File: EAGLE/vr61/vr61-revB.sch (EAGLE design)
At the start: 235 parts, among them J2 SM04B-SRSS-TB(LF)(SN), J6 MICROMOD-2222-C, Y1 74AHCT1G125

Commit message: wip 2022-07-21
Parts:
- removed J6: MICROMOD-2222-C, SparkFun-MicroMod:MICROMOD-2222-C
- added C12: 1mF, rcl:C-EUC0603
- added C13: 100nF, rcl:C-EUC0603
- added R7: 470, rcl:R-EU_R0603
- added R8: 5.1K, rcl:R-EU_R0603
- added W1: M25C, __untitled:M25C
- added X1: MICROMOD-2222-C, SparkFun-MicroMod:MICROMOD-2222-C
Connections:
- removed net N$70: LED-CL.4_DIN, Y1.Y_DOUT
- new net EE_CS: W1.!CS, X1.SPI_!CS!
- new net MISO: W1.DO, X1.SPI_SDI
- new net MOSI: W1.DIO, X1.SPI_SDO
- new net N$66: R7.2, Y1.Y_DOUT
- new net N$67: LED-CL.4_DIN, R7.1
- new net SCK: R8.2, W1.CLK, X1.SPI_SCK
- net !BOOT: now also X1.!BOOT!; no longer J6.!BOOT!
- net !RESET: now also X1.!RESET!; no longer J6.!RESET!
- net A0: now also X1.A0; no longer J6.A0
- net D+: now also X1.USB_D+; no longer J6.USB_D+
- net D-: now also X1.USB_D-; no longer J6.USB_D-
- net GND: now also C12.2, C13.2, R8.1, W1.GND, X1.GND; no longer J6.GND
- net LED: now also X1.PWM1; no longer J6.PWM1
- net MX0: now also X1.D1/CAM_TRIG; no longer J6.D1/CAM_TRIG
- net MX1: now also X1.I2C_!INT!; no longer J6.I2C_!INT!
- net MX2: now also X1.I2C_SCL; no longer J6.I2C_SCL
- net MX3: now also X1.A1; no longer J6.A1
- net MX4: now also X1.I2C_SDA; no longer J6.I2C_SDA
- net MX5: now also X1.D0; no longer J6.D0
- net MX6: now also X1.TX1; no longer J6.TX1
- net MX7: now also X1.RX1; no longer J6.RX1
- net MY0: now also X1.AUD_OUT/CAM_MCLK; no longer J6.AUD_OUT/CAM_MCLK
- net MY1: now also X1.AUD_IN/CAM_PCLK; no longer J6.AUD_IN/CAM_PCLK
- net MY2: now also X1.AUD_LRCLK; no longer J6.AUD_LRCLK
- net MY3: now also X1.AUD_BCLK; no longer J6.AUD_BCLK
- net MY4: now also X1.G4/BUS4; no longer J6.G4/BUS4
- net MY5: now also X1.G3/BUS3; no longer J6.G3/BUS3
- net MY6: now also X1.G2/BUS2; no longer J6.G2/BUS2
- net MY7: now also X1.G1/BUS1; no longer J6.G1/BUS1
- net MY8: now also X1.G0/BUS0; no longer J6.G0/BUS0
- net PWM: now also X1.PWM0; no longer J6.PWM0
- net SWDCK: now also X1.SWDCK; no longer J6.SWDCK
- net SWDIO: now also X1.SWDIO; no longer J6.SWDIO
- net VCC: now also C13.1, W1.!HLD, W1.!WP, W1.VCC, X1.3.3V, X1.3.3V_EN; no longer J6.3.3V, J6.3.3V_EN
- net VIN/3: now also X1.BATT_VIN/3; no longer J6.BATT_VIN/3
- net VSUP: now also C12.1, X1.USB_VIN; no longer J6.USB_VIN
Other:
- note added: "SPI EEPROM"
- moved on the sheet: C1, C10, C11, C2, C3, C4, C5, C7, C8, C9, D0, H5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

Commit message: wip 2022-07-21
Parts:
- removed Y1: 74AHCT1G125, ts_keyboards:74AHCT1G125
- removed Z1, Z10, Z11, Z12, Z13, Z16, Z17, Z18, Z19, Z2, Z20, Z21, Z22, Z23, Z24, Z25, Z26, Z27, Z3, Z30, Z31, Z32, Z33, Z34, Z35, Z36, Z37, Z38, Z39, Z4, Z40, Z43, Z44, Z45, Z46, Z47, Z48, Z49, Z5, Z50, Z51, Z52: MX-FPRINT-100U19, ts_keyboards:MX-FPRINT-100U19
- removed Z14: MX-FPRINT-200U19, ts_keyboards:MX-FPRINT-200U19
- removed Z15, Z28: MX-FPRINT-150U19, ts_keyboards:MX-FPRINT-150U19
- removed Z29: MX-FPRINT-175U19, ts_keyboards:MX-FPRINT-175U19
- removed Z41, Z42: MX-FPRINT-225U19, ts_keyboards:MX-FPRINT-225U19
- removed Z53: MX-FPRINT-275U19, ts_keyboards:MX-FPRINT-275U19
- removed Z54, Z55, Z56, Z58, Z59, Z60, Z61: MX-FPRINT-125U19, ts_keyboards:MX-FPRINT-125U19
- removed Z57: MX-FPRINT-625U19, ts_keyboards:MX-FPRINT-625U19
- added IC1: MC74VHC1G50SC-74A, ts_keyboards:MC74VHC1G50SC-74A
- renumbered B14 to T_BSPC, B41 to T_ENT, B42 to T_LSFT, B53 to T_RSFT, B57 to T_SPC, S_BSL to S_BSLS, S_BSP to S_BSPC, S_CB to S_RBRC, S_CPS to S_CAPS, S_FSL to S_SLSH, S_LAL to S_LALT, S_LCT to S_LCTL, S_LGU to S_LGUI, S_LSH to S_LSFT, S_MIN to S_MINS, S_OB to S_LBRC, S_QUO to S_QUOT, S_RAL to S_APP, S_RCT to S_RCTL, S_RGU to S_RALT, S_RSH to S_RSFT, S_SCL to S_SCLN
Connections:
- net GND: now also IC1.3_GND; no longer Y1.!OE, Y1.3_GND
- net LED1ST: now also IC1.A_DIN; no longer Y1.A_DIN
- net N$66: now also IC1.Y_DOUT; no longer Y1.Y_DOUT
- net VSUP: now also IC1.5_VCC; no longer Y1.5_VCC

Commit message: wip 2022-07-22
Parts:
- removed SA1, SA2, SA3, SC2: MOUNTING-HOLE-WIDE, ts_keyboards:MOUNTING-HOLE-WIDE
- removed SC1: MOUNTING-HOLE, ts_keyboards:MOUNTING-HOLE
- removed SG1, SG4: MOUNTING-HOLE-VWIDEEDGE-CUT, ts_keyboards:MOUNTING-HOLE-VWIDEEDGE-CUT
- added FP_AP2: FOOTPRINT-AP2, ts_keyboards:FOOTPRINT-AP2
- added FP_GH60: FOOTPRINT-GH60, ts_keyboards:FOOTPRINT-GH60
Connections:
- removed net SA1: SA1.P$1
- removed net SA2: SA2.P$1
- removed net SA3: SA3.P$1
- removed net SC2: SC2.P$1
- removed net SG1: SG1.P$1
- removed net SG4: SG4.P$1
- net SC1: no longer SC1.P$1
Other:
- note added: "TE P# 2199119-4"
- moved on the sheet: J3, JP2

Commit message: final touches and validation for rev B
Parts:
- removed IC1: MC74VHC1G50SC-74A, ts_keyboards:MC74VHC1G50SC-74A
- added D62: (no value), jlcpcb_basic_parts:1N5819WS
- added J6: (no value), SparkFun-Connectors:CONN_01
- added J7: (no value), SparkFun-Connectors:CONN_02
- added S_BSLS2, S_ENT2, S_LSFT2, S_NUBS: MX-5-PIN-HOTSWAP-PADNO-SILK, ts_keyboards:MX-5-PIN-HOTSWAP-PADNO-SILK
- added T_ENT1: MX-STABS-200U, ts_keyboards:MX-STABS-200U
- added U$14: 74AHCT1G125GV, ts_keyboards:74AHCT1G125GV
- J3: device SparkFun-Connectors:CONN_04 -> SparkFun-Connectors:CONN_03
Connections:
- removed net A0: J3.3, X1.A0
- removed net PWM: J3.2, X1.PWM0
- removed net SINK: LM1117.OUT@1
- removed net SWDCK: X1.SWDCK
- removed net SWDIO: X1.SWDIO
- new net 52: J3.2, X1.AUD_LRCLK
- new net 63: J6.1, X1.G10/ADC_D+/CAM_VSYNC
- new net N$69: D43.A, S_NUBS.P
- new net USBHOST_D+: J7.1, X1.USBHOST_D+
- new net USBHOST_D-: J7.2, X1.USBHOST_D-
- net GND: now also U$14.!OE, U$14.3_GND; no longer IC1.3_GND
- net LED: now also X1.PWM0; no longer X1.PWM1
- net LED1ST: now also U$14.A_DIN; no longer IC1.A_DIN
- net MX0: now also D50.C, D55.C, X1.PWM1; no longer D49.C, D54.C, X1.D1/CAM_TRIG
- net MX1: now also D43.C, D51.C, D56.C, X1.RX1; no longer D50.C, D55.C, X1.I2C_!INT!
- net MX2: now also D44.C, D52.C, D57.C, X1.TX1; no longer D43.C, D51.C, D56.C, X1.I2C_SCL
- net MX3: now also D45.C, D53.C, D58.C, X1.D1/CAM_TRIG; no longer D44.C, D52.C, D57.C, X1.A1
- net MX4: now also D46.C, D59.C, X1.I2C_!INT!; no longer D45.C, D58.C, X1.I2C_SDA
- net MX5: now also D47.C, D54.C, D60.C, X1.I2C_SCL; no longer D46.C, D53.C, D59.C, X1.D0
- net MX6: now also D48.C, D61.C, X1.I2C_SDA; no longer D47.C, D60.C, X1.TX1
- net MX7: now also D49.C, D62.C, X1.D0; no longer D48.C, D61.C, X1.RX1
- net MY2: now also X1.AUD_BCLK; no longer X1.AUD_LRCLK
- net MY3: now also S_LSFT2.S, S_NUBS.S, X1.G3/BUS3; no longer X1.AUD_BCLK
- net MY4: now also X1.G2/BUS2; no longer X1.G4/BUS4
- net MY5: now also X1.G1/BUS1; no longer X1.G3/BUS3
- net MY6: now also S_BSLS2.S, X1.G0/BUS0; no longer X1.G2/BUS2
- net MY7: now also S_ENT2.S, X1.A1; no longer X1.G1/BUS1
- net MY8: now also X1.A0; no longer X1.G0/BUS0
- net N$28: now also S_BSLS2.P
- net N$41: now also S_ENT2.P
- net N$42: now also S_LSFT2.P
- net N$43: now also D44.A; no longer D43.A
- net N$44: now also D45.A; no longer D44.A
- net N$45: now also D46.A; no longer D45.A
- net N$46: now also D47.A; no longer D46.A
- net N$47: now also D48.A; no longer D47.A
- net N$48: now also D49.A; no longer D48.A
- net N$49: now also D50.A; no longer D49.A
- net N$50: now also D51.A; no longer D50.A
- net N$51: now also D52.A; no longer D51.A
- net N$52: now also D53.A; no longer D52.A
- net N$53: now also D54.A; no longer D53.A
- net N$54: now also D55.A; no longer D54.A
- net N$55: now also D56.A; no longer D55.A
- net N$56: now also D57.A; no longer D56.A
- net N$57: now also D58.A; no longer D57.A
- net N$58: now also D59.A; no longer D58.A
- net N$59: now also D60.A; no longer D59.A
- net N$60: now also D61.A; no longer D60.A
- net N$61: now also D62.A; no longer D61.A
- net N$66: now also U$14.Y_DOUT; no longer IC1.Y_DOUT
- net VCC: now also J3.3; no longer J3.4
- net VSUP: now also U$14.5_VCC; no longer IC1.5_VCC
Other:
- moved on the sheet: D43, D44, D45, D46, D47, D48, D49, D50, D51, D52, D53, D54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

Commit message: updates after production prep
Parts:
- C12: value 1mF -> 0.1uF
- renumbered C1 to C01, C2 to C02, C3 to C03, C4 to C04, C5 to C05, C6 to C06, C7 to C07, C8 to C08, C9 to C09, D0 to D00, D1 to D01, D2 to D02, D3 to D03, D4 to D04, D5 to D05, D6 to D06, D7 to D07, D8 to D08, D9 to D09, J1 to J-BOOT, J2 to J-UDB, J3 to J-52, J4 to J-LED, J5 to J-UBS, J6 to J-63, J7 to J-HOST, JP1 to JP-VIN3, JP2 to JP-GND, W1 to M1

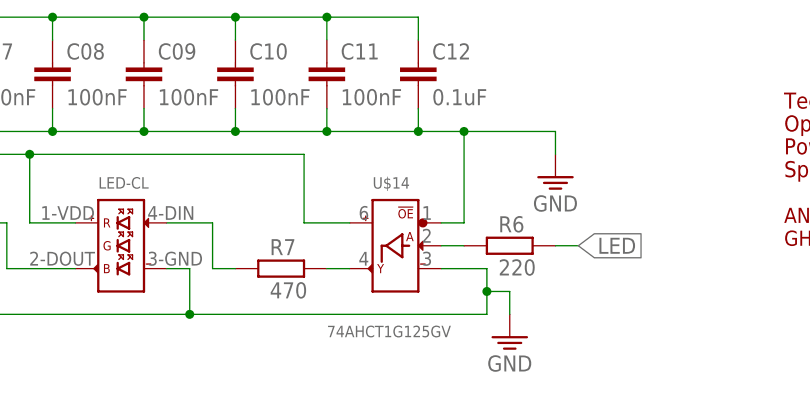
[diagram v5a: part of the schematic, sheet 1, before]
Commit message: 74AHCT1G125GW
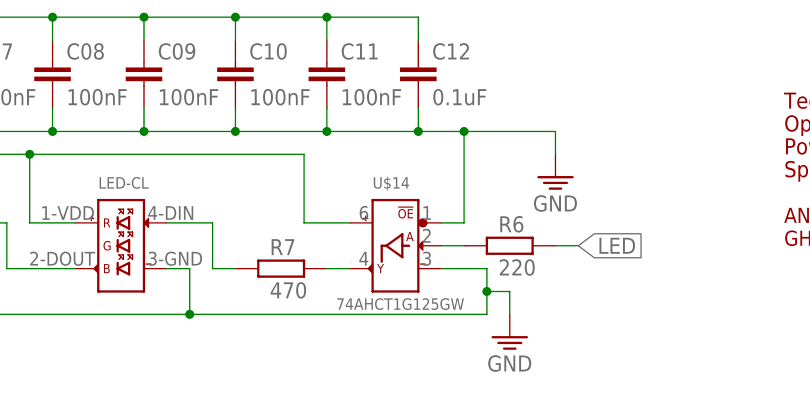
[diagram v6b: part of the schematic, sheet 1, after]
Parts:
- U$14: value 74AHCT1G125GV -> 74AHCT1G125GW; device ts_keyboards:74AHCT1G125GV -> ts_keyboards:74AHCT1G125GW
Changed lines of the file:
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@@
 <part name="S_ENT2" library="ts_keyboards" deviceset="MX-5-PIN-HOTSWAP-PAD" device="NO-SILK"/>
 <part name="S_BSLS2" library="ts_keyboards" deviceset="MX-5-PIN-HOTSWAP-PAD" device="NO-SILK"/>
-<part name="U$14" library="ts_keyboards" deviceset="74AHCT1G125GV" device=""/>
 <part name="J-HOST" library="SparkFun-Connectors" library_urn="urn:adsk.eagle:library:513" deviceset="CONN_02" device="" package3d_urn="urn:adsk.eagle:package:38039/1"/>
 <part name="J-63" library="SparkFun-Connectors" library_urn="urn:adsk.eagle:library:513" deviceset="CONN_01" device="" package3d_urn="urn:adsk.eagle:package:38028/1"/>
 <part name="T_ENT1" library="ts_keyboards" deviceset="MX-STABS-200U" device=""/>
 <part name="J-52" library="SparkFun-Connectors" library_urn="urn:adsk.eagle:library:513" deviceset="CONN_03" device="" package3d_urn="urn:adsk.eagle:package:38063/1"/>
+<part name="U$14" library="ts_keyboards" deviceset="74AHCT1G125GW" device=""/>
 </parts>
 <sheets>
@@
 <instance part="FP_AP2" gate="G$1" x="193.04" y="17.78" smashed="yes"/>
 <instance part="FP_GH60" gate="G$1" x="193.04" y="15.24" smashed="yes"/>
-<instance part="U$14" gate="G$1" x="149.86" y="15.24" smashed="yes">
-<attribute name="NAME" x="147.32" y="21.59" size="1.27" layer="95"/>
-<attribute name="VALUE" x="142.24" y="5.08" size="1.27" layer="96"/>
-</instance>
 <instance part="J-HOST" gate="G$1" x="160.02" y="124.46" smashed="yes">
 <attribute name="VALUE" x="157.48" y="119.634" size="1.778" layer="96" font="vector"/>
@@
 <attribute name="VALUE" x="236.22" y="51.054" size="1.778" layer="96" font="vector"/>
 <attribute name="NAME" x="236.22" y="64.008" size="1.778" layer="95" font="vector"/>
+</instance>
+<instance part="U$14" gate="G$1" x="149.86" y="15.24" smashed="yes">
+<attribute name="NAME" x="147.32" y="21.59" size="1.27" layer="95"/>
+<attribute name="VALUE" x="143.256" y="8.128" size="1.27" layer="96"/>
 </instance>
 </instances>
@@
 </segment>
 <segment>
+<pinref part="GND12" gate="1" pin="GND"/>
+<wire x1="71.12" y1="35.56" x2="71.12" y2="38.1" width="0.1524" layer="91"/>
+<wire x1="71.12" y1="38.1" x2="81.28" y2="38.1" width="0.1524" layer="91"/>
+<pinref part="C13" gate="G$1" pin="2"/>
+<wire x1="81.28" y1="38.1" x2="81.28" y2="43.18" width="0.1524" layer="91"/>
+<wire x1="71.12" y1="38.1" x2="45.72" y2="38.1" width="0.1524" layer="91"/>
+<junction x="71.12" y="38.1"/>
+<wire x1="45.72" y1="38.1" x2="45.72" y2="43.18" width="0.1524" layer="91"/>
+<pinref part="M1" gate="G$1" pin="GND"/>
+<wire x1="45.72" y1="43.18" x2="48.26" y2="43.18" width="0.1524" layer="91"/>
+</segment>
+<segment>
+<pinref part="R8" gate="G$1" pin="1"/>
+<wire x1="246.38" y1="142.24" x2="248.92" y2="142.24" width="0.1524" layer="91"/>
+<pinref part="GND13" gate="1" pin="GND"/>
+<wire x1="248.92" y1="142.24" x2="248.92" y2="139.7" width="0.1524" layer="91"/>
+</segment>
+<segment>
 <pinref part="C07" gate="G$1" pin="2"/>
 <pinref part="C08" gate="G$1" pin="2"/>
@@
 <wire x1="167.64" y1="25.4" x2="167.64" y2="27.94" width="0.1524" layer="91"/>
 <wire x1="167.64" y1="27.94" x2="157.48" y2="27.94" width="0.1524" layer="91"/>
-<pinref part="U$14" gate="G$1" pin="!OE"/>
 <wire x1="157.48" y1="27.94" x2="152.4" y2="27.94" width="0.1524" layer="91"/>
-<wire x1="154.94" y1="17.78" x2="157.48" y2="17.78" width="0.1524" layer="91"/>
 <wire x1="157.48" y1="17.78" x2="157.48" y2="27.94" width="0.1524" layer="91"/>
 <junction x="157.48" y="27.94"/>
-</segment>
-<segment>
-<pinref part="GND12" gate="1" pin="GND"/>
-<wire x1="71.12" y1="35.56" x2="71.12" y2="38.1" width="0.1524" layer="91"/>
-<wire x1="71.12" y1="38.1" x2="81.28" y2="38.1" width="0.1524" layer="91"/>
-<pinref part="C13" gate="G$1" pin="2"/>
-<wire x1="81.28" y1="38.1" x2="81.28" y2="43.18" width="0.1524" layer="91"/>
-<wire x1="71.12" y1="38.1" x2="45.72" y2="38.1" width="0.1524" layer="91"/>
-<junction x="71.12" y="38.1"/>
-<wire x1="45.72" y1="38.1" x2="45.72" y2="43.18" width="0.1524" layer="91"/>
-<pinref part="M1" gate="G$1" pin="GND"/>
-<wire x1="45.72" y1="43.18" x2="48.26" y2="43.18" width="0.1524" layer="91"/>
-</segment>
-<segment>
-<pinref part="R8" gate="G$1" pin="1"/>
-<wire x1="246.38" y1="142.24" x2="248.92" y2="142.24" width="0.1524" layer="91"/>
-<pinref part="GND13" gate="1" pin="GND"/>
-<wire x1="248.92" y1="142.24" x2="248.92" y2="139.7" width="0.1524" layer="91"/>
+<pinref part="U$14" gate="G$1" pin="!OE"/>
+<wire x1="157.48" y1="17.78" x2="154.94" y2="17.78" width="0.1524" layer="91"/>
 </segment>
 </net>
